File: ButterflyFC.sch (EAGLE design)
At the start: 6 parts

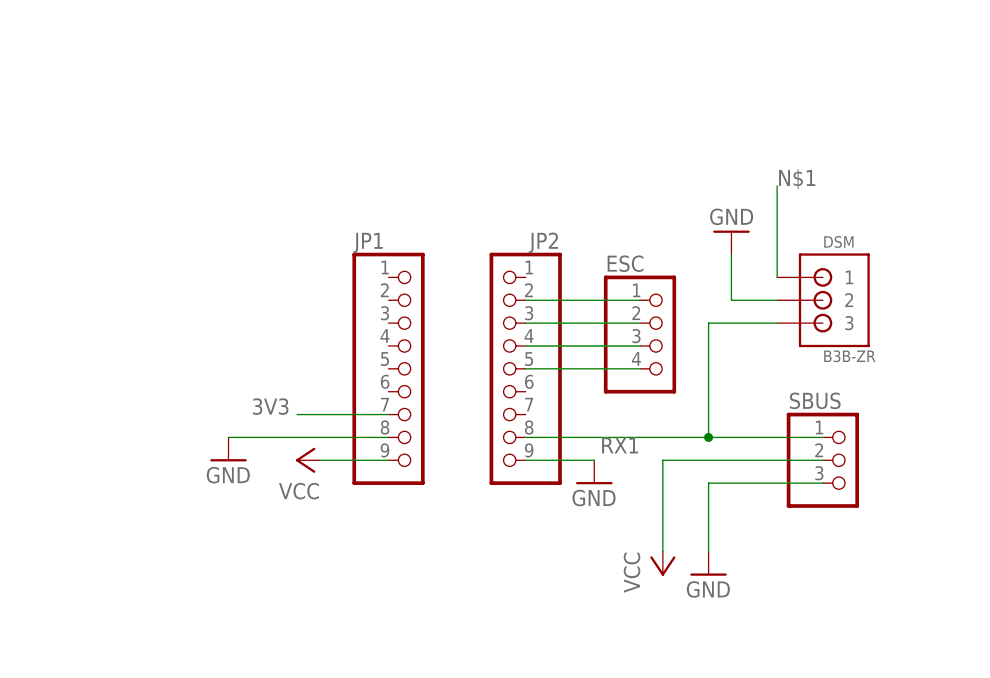
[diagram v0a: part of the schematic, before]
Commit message: Added ESC power rail
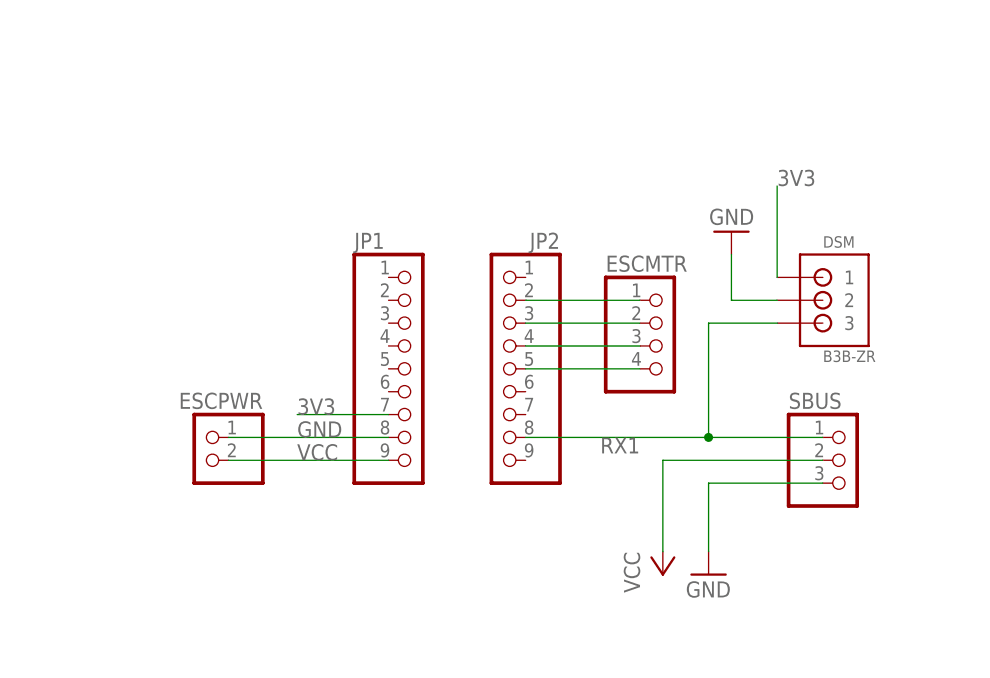
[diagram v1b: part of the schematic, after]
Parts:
- added ESCPWR: (no value), pinhead:PINHD-1X2/90
- renumbered ESC to ESCMTR
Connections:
- net GND: now also ESCPWR.1; no longer JP2.9
- net VCC: now also ESCPWR.2
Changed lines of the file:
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@@
 <part name="JP1" library="pinhead" library_urn="urn:adsk.eagle:library:325" deviceset="PINHD-1X9" device="" package3d_urn="urn:adsk.eagle:package:22483/2"/>
 <part name="JP2" library="pinhead" library_urn="urn:adsk.eagle:library:325" deviceset="PINHD-1X9" device="" package3d_urn="urn:adsk.eagle:package:22483/2"/>
-<part name="GND1" library="supply1" library_urn="urn:adsk.eagle:library:371" deviceset="GND" device=""/>
-<part name="VIN" library="supply1" library_urn="urn:adsk.eagle:library:371" deviceset="VCC" device=""/>
-<part name="GND2" library="supply1" library_urn="urn:adsk.eagle:library:371" deviceset="GND" device=""/>
 <part name="SBUS" library="pinhead" library_urn="urn:adsk.eagle:library:325" deviceset="PINHD-1X3" device="" package3d_urn="urn:adsk.eagle:package:22458/2"/>
 <part name="P+2" library="supply1" library_urn="urn:adsk.eagle:library:371" deviceset="VCC" device=""/>
 <part name="GND3" library="supply1" library_urn="urn:adsk.eagle:library:371" deviceset="GND" device=""/>
-<part name="ESC" library="pinhead" library_urn="urn:adsk.eagle:library:325" deviceset="PINHD-1X4" device="" package3d_urn="urn:adsk.eagle:package:22407/2"/>
+<part name="ESCMTR" library="pinhead" library_urn="urn:adsk.eagle:library:325" deviceset="PINHD-1X4" device="" package3d_urn="urn:adsk.eagle:package:22407/2"/>
 <part name="DSM" library="jst" deviceset="B3B-ZR" device=""/>
 <part name="GND4" library="supply1" library_urn="urn:adsk.eagle:library:371" deviceset="GND" device=""/>
+<part name="ESCPWR" library="pinhead" library_urn="urn:adsk.eagle:library:325" deviceset="PINHD-1X2" device="/90" package3d_urn="urn:adsk.eagle:package:22437/2"/>
 </parts>
 <sheets>
@@
 <instance part="JP1" gate="A" x="109.22" y="83.82"/>
 <instance part="JP2" gate="A" x="119.38" y="83.82" rot="MR0"/>
-<instance part="GND1" gate="1" x="88.9" y="73.66"/>
-<instance part="VIN" gate="VCC" x="96.52" y="73.66" rot="R90"/>
-<instance part="GND2" gate="1" x="129.54" y="71.12"/>
 <instance part="SBUS" gate="A" x="157.48" y="73.66"/>
 <instance part="P+2" gate="VCC" x="137.16" y="60.96" rot="MR180"/>
 <instance part="GND3" gate="1" x="142.24" y="60.96"/>
-<instance part="ESC" gate="A" x="137.16" y="86.36"/>
+<instance part="ESCMTR" gate="A" x="137.16" y="86.36"/>
 <instance part="DSM" gate="G$1" x="157.48" y="91.44"/>
 <instance part="GND4" gate="1" x="144.78" y="99.06" rot="R180"/>
+<instance part="ESCPWR" gate="G$1" x="86.36" y="73.66" rot="MR0"/>
 </instances>
 <busses>
@@
 <nets>
 <net name="GND" class="0">
-<segment>
-<pinref part="JP2" gate="A" pin="9"/>
-<pinref part="GND2" gate="1" pin="GND"/>
-<wire x1="121.92" y1="73.66" x2="129.54" y2="73.66" width="0.1524" layer="91"/>
-</segment>
 <segment>
 <pinref part="SBUS" gate="A" pin="3"/>
@@
 </segment>
 <segment>
-<pinref part="GND1" gate="1" pin="GND"/>
 <pinref part="JP1" gate="A" pin="8"/>
-<wire x1="88.9" y1="76.2" x2="106.68" y2="76.2" width="0.1524" layer="91"/>
+<pinref part="ESCPWR" gate="G$1" pin="1"/>
+<wire x1="106.68" y1="76.2" x2="88.9" y2="76.2" width="0.1524" layer="91"/>
+<label x="96.52" y="76.2" size="1.778" layer="95"/>
 </segment>
 </net>
 <net name="VCC" class="0">
-<segment>
-<pinref part="VIN" gate="VCC" pin="VCC"/>
-<pinref part="JP1" gate="A" pin="9"/>
-<wire x1="99.06" y1="73.66" x2="106.68" y2="73.66" width="0.1524" layer="91"/>
-</segment>
 <segment>
 <pinref part="P+2" gate="VCC" pin="VCC"/>
@@
 <pinref part="SBUS" gate="A" pin="2"/>
 <wire x1="137.16" y1="73.66" x2="154.94" y2="73.66" width="0.1524" layer="91"/>
+</segment>
+<segment>
+<pinref part="JP1" gate="A" pin="9"/>
+<pinref part="ESCPWR" gate="G$1" pin="2"/>
+<wire x1="106.68" y1="73.66" x2="88.9" y2="73.66" width="0.1524" layer="91"/>
+<label x="96.52" y="73.66" size="1.778" layer="95"/>
 </segment>
 </net>
@@
 <segment>
 <pinref part="JP2" gate="A" pin="5"/>
-<pinref part="ESC" gate="A" pin="4"/>
+<pinref part="ESCMTR" gate="A" pin="4"/>
 <wire x1="121.92" y1="83.82" x2="134.62" y2="83.82" width="0.1524" layer="91"/>
 </segment>
@@
 <segment>
 <pinref part="JP2" gate="A" pin="2"/>
-<pinref part="ESC" gate="A" pin="1"/>
+<pinref part="ESCMTR" gate="A" pin="1"/>
 <wire x1="121.92" y1="91.44" x2="134.62" y2="91.44" width="0.1524" layer="91"/>
 </segment>
@@
 <net name="N$6" class="0">
 <segment>
-<pinref part="ESC" gate="A" pin="3"/>
+<pinref part="ESCMTR" gate="A" pin="3"/>
 <pinref part="JP2" gate="A" pin="4"/>
 <wire x1="121.92" y1="86.36" x2="134.62" y2="86.36" width="0.1524" layer="91"/>
@@
 <pinref part="JP1" gate="A" pin="7"/>
 <wire x1="106.68" y1="78.74" x2="96.52" y2="78.74" width="0.1524" layer="91"/>
-<label x="91.44" y="78.74" size="1.778" layer="95"/>
+<label x="96.52" y="78.74" size="1.778" layer="95"/>
+<label x="149.86" y="104.14" size="1.778" layer="95"/>
 </segment>
 </net>
@@
 <pinref part="DSM" gate="G$1" pin="1"/>
 <wire x1="149.86" y1="93.98" x2="149.86" y2="104.14" width="0.1524" layer="91"/>
-<label x="149.86" y="104.14" size="1.778" layer="95"/>
 </segment>
 </net>

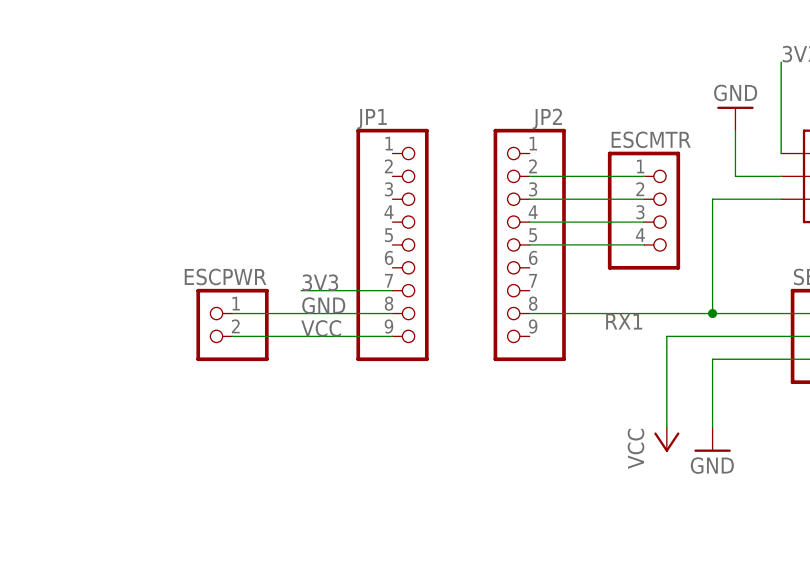
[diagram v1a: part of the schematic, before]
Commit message: Routed board
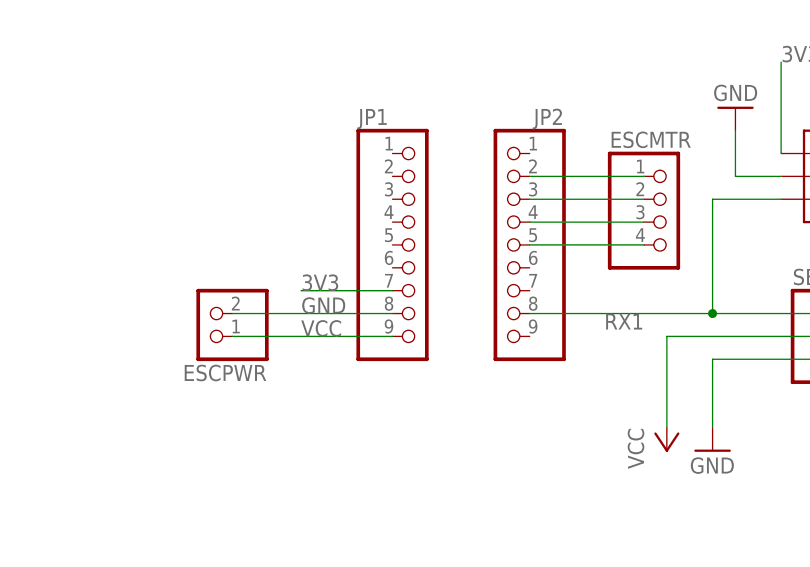
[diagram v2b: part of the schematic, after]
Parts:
- ESCPWR: device pinhead:PINHD-1X2/90 -> pinhead:PINHD-1X2
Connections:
- net GND: now also ESCPWR.2; no longer ESCPWR.1
- net N$4: now also ESCMTR.2
- net VCC: now also ESCPWR.1; no longer ESCPWR.2
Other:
- moved on the sheet: ESCPWR
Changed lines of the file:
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@@
 <part name="DSM" library="jst" deviceset="B3B-ZR" device=""/>
 <part name="GND4" library="supply1" library_urn="urn:adsk.eagle:library:371" deviceset="GND" device=""/>
-<part name="ESCPWR" library="pinhead" library_urn="urn:adsk.eagle:library:325" deviceset="PINHD-1X2" device="/90" package3d_urn="urn:adsk.eagle:package:22437/2"/>
+<part name="ESCPWR" library="pinhead" library_urn="urn:adsk.eagle:library:325" deviceset="PINHD-1X2" device="" package3d_urn="urn:adsk.eagle:package:22435/2"/>
 </parts>
 <sheets>
@@
 <instance part="DSM" gate="G$1" x="157.48" y="91.44"/>
 <instance part="GND4" gate="1" x="144.78" y="99.06" rot="R180"/>
-<instance part="ESCPWR" gate="G$1" x="86.36" y="73.66" rot="MR0"/>
+<instance part="ESCPWR" gate="G$1" x="86.36" y="76.2" rot="R180"/>
 </instances>
 <busses>
@@
 <segment>
 <pinref part="JP1" gate="A" pin="8"/>
-<pinref part="ESCPWR" gate="G$1" pin="1"/>
 <wire x1="106.68" y1="76.2" x2="88.9" y2="76.2" width="0.1524" layer="91"/>
 <label x="96.52" y="76.2" size="1.778" layer="95"/>
+<pinref part="ESCPWR" gate="G$1" pin="2"/>
 </segment>
 </net>
@@
 <segment>
 <pinref part="JP1" gate="A" pin="9"/>
-<pinref part="ESCPWR" gate="G$1" pin="2"/>
 <wire x1="106.68" y1="73.66" x2="88.9" y2="73.66" width="0.1524" layer="91"/>
 <label x="96.52" y="73.66" size="1.778" layer="95"/>
+<pinref part="ESCPWR" gate="G$1" pin="1"/>
 </segment>
 </net>
@@
 <pinref part="ESCMTR" gate="A" pin="4"/>
 <wire x1="121.92" y1="83.82" x2="134.62" y2="83.82" width="0.1524" layer="91"/>
-</segment>
-</net>
-<net name="N$4" class="0">
-<segment>
-<pinref part="JP2" gate="A" pin="3"/>
-<wire x1="121.92" y1="88.9" x2="134.62" y2="88.9" width="0.1524" layer="91"/>
-</segment>
-</net>
-<net name="N$5" class="0">
-<segment>
-<pinref part="JP2" gate="A" pin="2"/>
-<pinref part="ESCMTR" gate="A" pin="1"/>
-<wire x1="121.92" y1="91.44" x2="134.62" y2="91.44" width="0.1524" layer="91"/>
 </segment>
 </net>
@@
 </segment>
 </net>
+<net name="N$2" class="0">
+<segment>
+<pinref part="ESCMTR" gate="A" pin="1"/>
+<pinref part="JP2" gate="A" pin="2"/>
+<wire x1="134.62" y1="91.44" x2="121.92" y2="91.44" width="0.1524" layer="91"/>
+</segment>
+</net>
+<net name="N$4" class="0">
+<segment>
+<pinref part="ESCMTR" gate="A" pin="2"/>
+<pinref part="JP2" gate="A" pin="3"/>
+<wire x1="134.62" y1="88.9" x2="121.92" y2="88.9" width="0.1524" layer="91"/>
+</segment>
+</net>

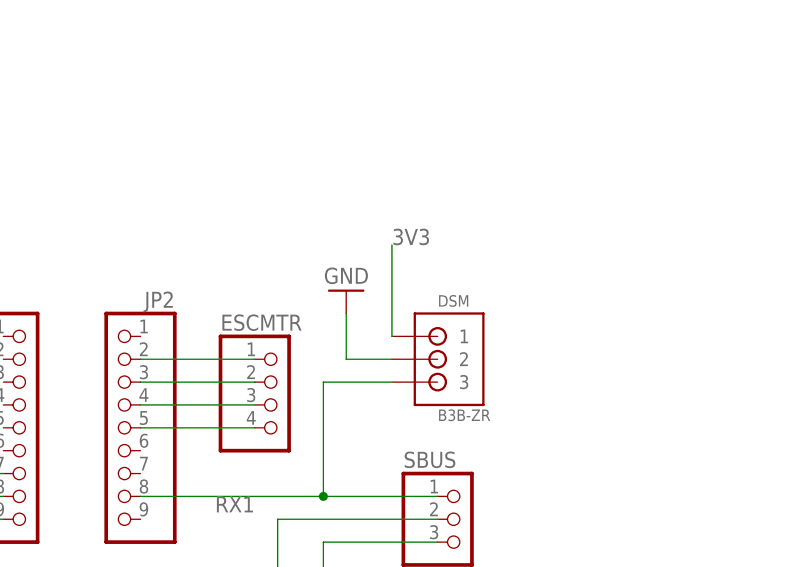
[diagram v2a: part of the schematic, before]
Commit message: Fixed broken 3.3V connection
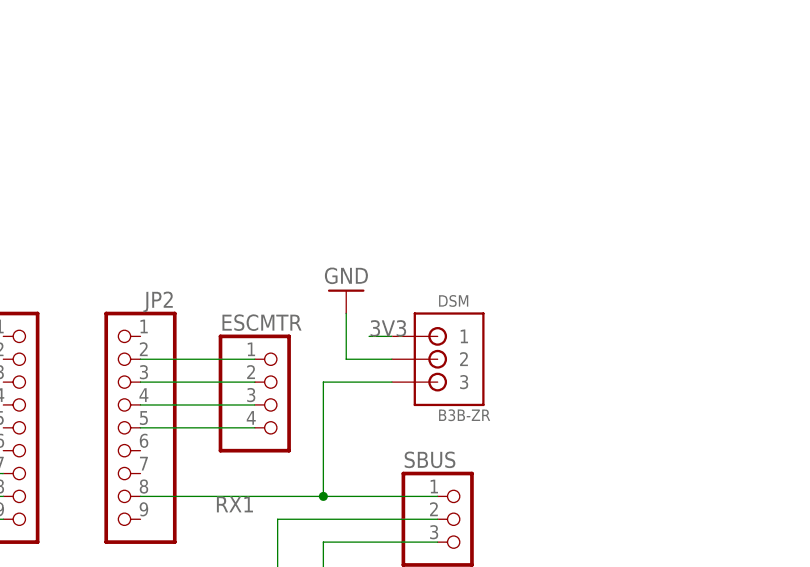
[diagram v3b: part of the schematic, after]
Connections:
- removed net N$1: DSM.1
- net 3V3: now also DSM.1
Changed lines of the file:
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@@
-</segment>
-</net>
-<net name="3V3" class="0">
-<segment>
-<pinref part="JP1" gate="A" pin="7"/>
-<wire x1="106.68" y1="78.74" x2="96.52" y2="78.74" width="0.1524" layer="91"/>
-<label x="96.52" y="78.74" size="1.778" layer="95"/>
-<label x="149.86" y="104.14" size="1.778" layer="95"/>
-</segment>
-</net>
-<net name="N$1" class="0">
-<segment>
-<pinref part="DSM" gate="G$1" pin="1"/>
-<wire x1="149.86" y1="93.98" x2="149.86" y2="104.14" width="0.1524" layer="91"/>
 </segment>
 </net>
@@
 </segment>
 </net>
+<net name="3V3" class="0">
+<segment>
+<pinref part="JP1" gate="A" pin="7"/>
+<wire x1="106.68" y1="78.74" x2="96.52" y2="78.74" width="0.1524" layer="91"/>
+<label x="96.52" y="78.74" size="1.778" layer="95"/>
+</segment>
+<segment>
+<pinref part="DSM" gate="G$1" pin="1"/>
+<wire x1="149.86" y1="93.98" x2="147.32" y2="93.98" width="0.1524" layer="91"/>
+<label x="147.32" y="93.98" size="1.778" layer="95"/>
+</segment>
+</net>
